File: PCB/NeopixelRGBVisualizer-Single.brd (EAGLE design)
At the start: 26.8 x 29.6 mm, 19 parts, among them IC1 MSGEQ7, Q1 16MHz, X1 STEREOJACK, X2 1751251

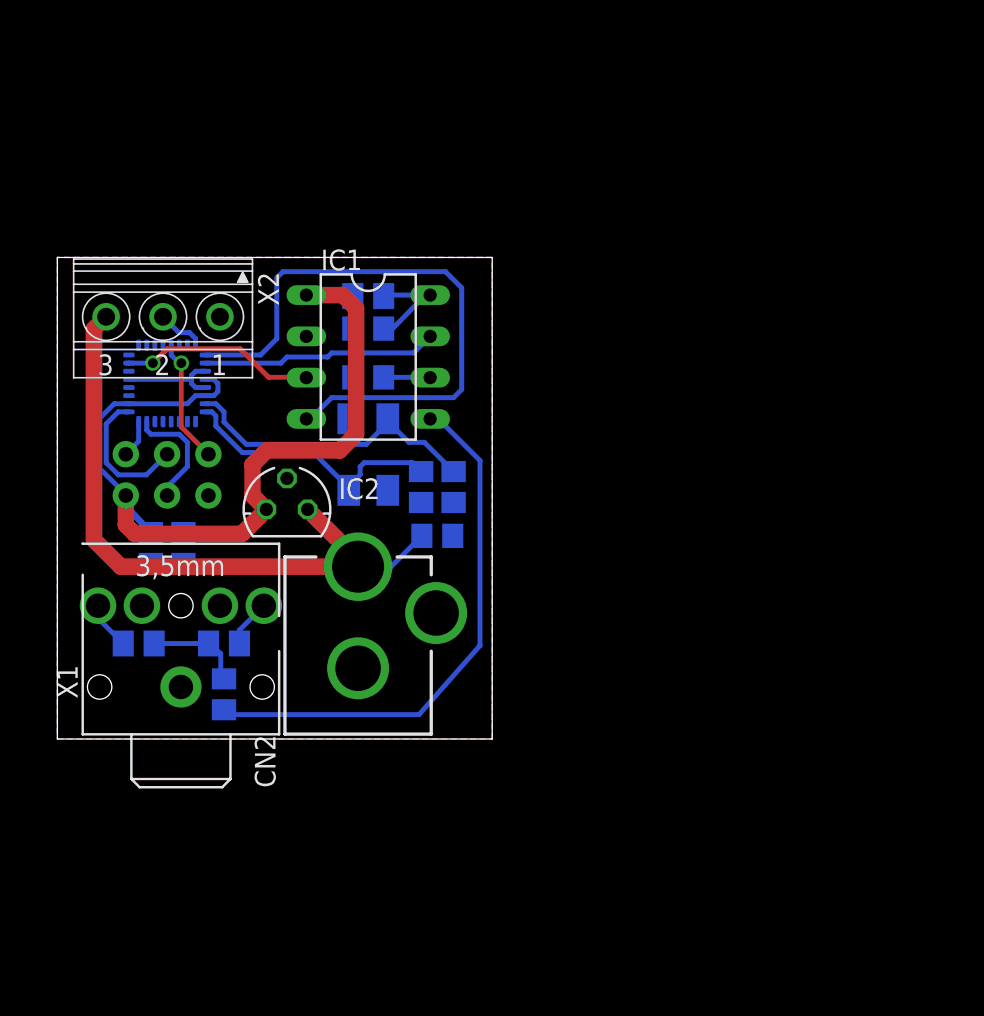
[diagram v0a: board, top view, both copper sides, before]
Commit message: Almost ready for second prototype order -Added 3 tactile buttons for control inputs: "Power","+","-" -Changed Phoenix screw terminal to Molex Mini-Fit Jr receptacle -Added small potentiometer as input volume control -Aligned receptacles with board edge
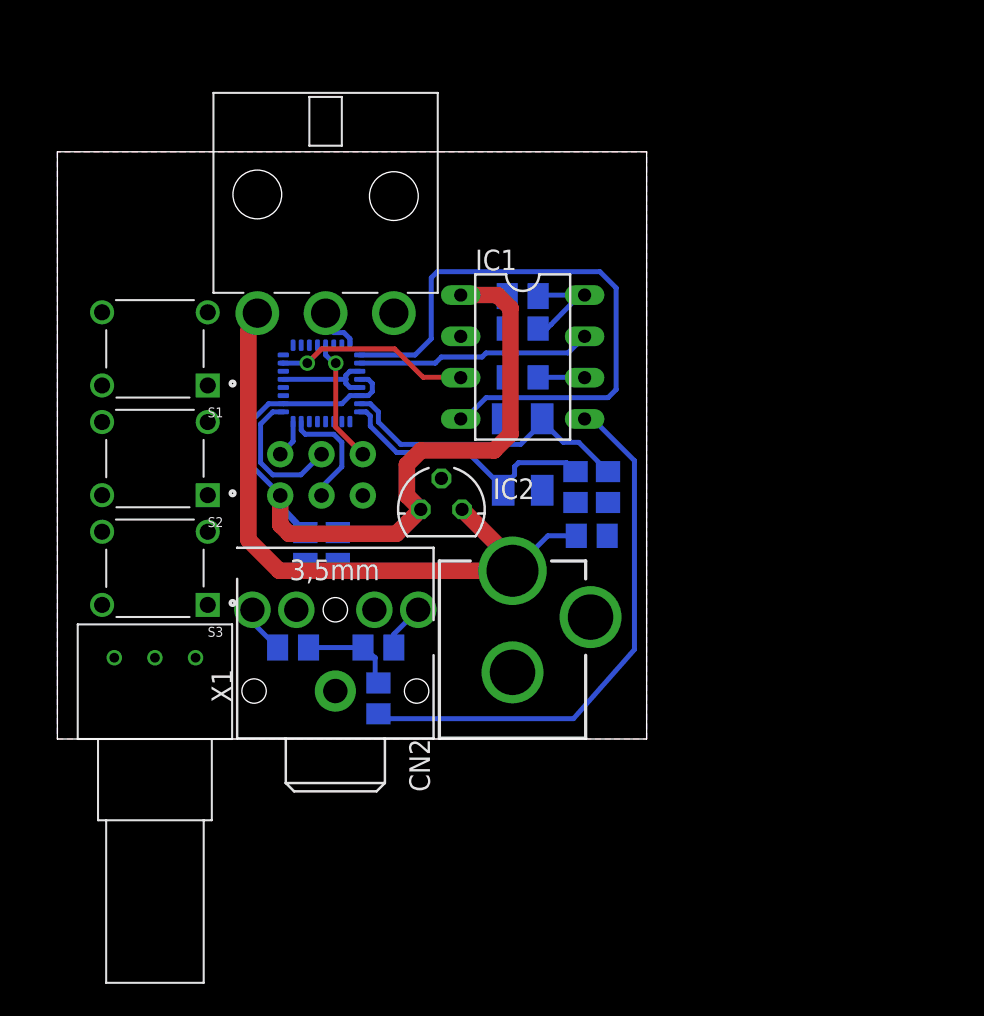
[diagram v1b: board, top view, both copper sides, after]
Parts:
- removed X2: 1751251, con-phoenix-350:1751251
- added S1, S2, S3: 2-1825910-7, 2-1825910-7:SW_2-1825910-7
- added U$2: PTD901-2015K, potentiometers:PTD901-2015K-####
- added U$3: 0039303035, MinifitJR:4.2MM-3PIN
- moved C1 9.50 mm to (19.8, 2.50)
- moved CN2 9.50 mm to (28.0, -3.25)
- moved R1 9.50 mm to (19.8, 5.62)
- moved R2 9.50 mm to (14.5, 5.62)
- moved X1 9.50 mm to (17.0, 0.25)
- moved C2 9.50 mm to (28.6, 25.2)
- moved C3 9.50 mm to (17.2, 11.8)
- moved C4 9.50 mm to (28.6, 22.2)
- moved C5 9.50 mm to (33.9, 15.5)
- moved C6 9.50 mm to (31.9, 15.5)
- moved C7 9.50 mm to (15.2, 11.8)
- moved C8 9.50 mm to (32.9, 12.5)
- moved IC1 9.50 mm to (28.6, 23.5)
- moved IC2 9.50 mm to (23.6, 14.1)
- moved ISP1 9.50 mm to (16.2, 16.2)
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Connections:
- new net N$16: C1.1, U$2.P$2
- new net N$18: S1.1, S1.2
- new net N$19: S2.1, S2.2
- new net N$20: S3.1, S3.2
- net GND: now also S1.3, S1.4, S2.3, S2.4, S3.3, S3.4, U$2.P$1, U$3.P$3; no longer X2.1
- net N$17: now also U$3.P$2; no longer X2.2
- net N$6: now also U$2.P$3; no longer C1.1
- net VIN: now also U$3.P$1; no longer X2.3
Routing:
- net N$17: track 2.96 -> 1.58 mm
- net VIN: track 40.5 -> 39.9 mm
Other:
- board size 26.8 x 29.6 mm -> 36.2 x 36.1 mm

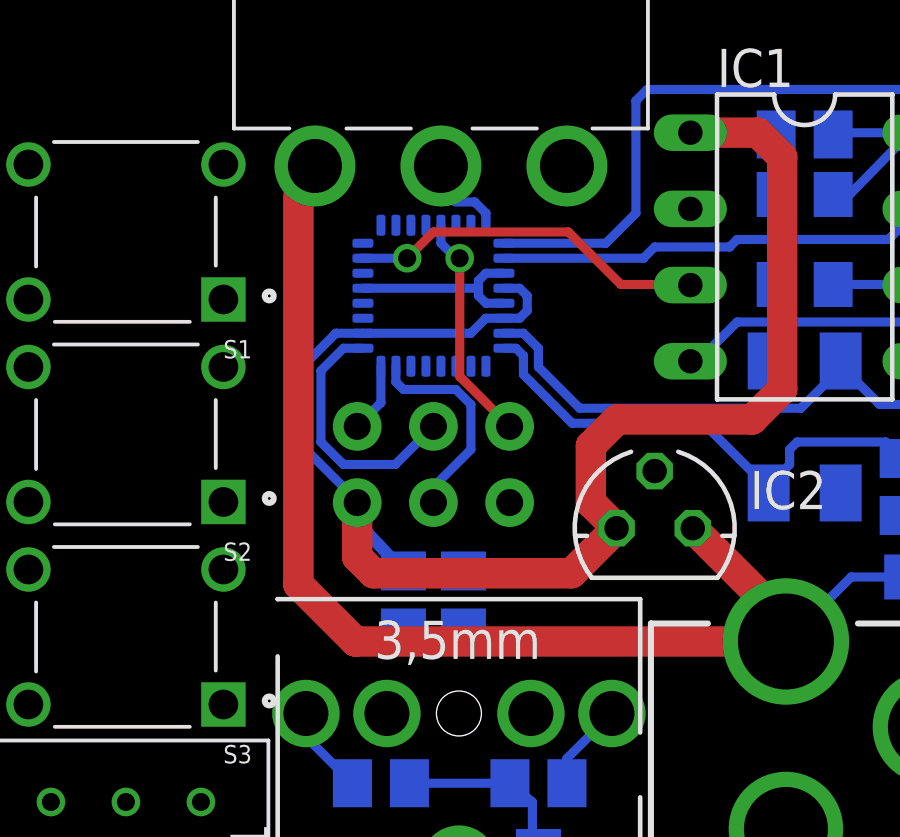
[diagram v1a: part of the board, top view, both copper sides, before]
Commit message: Reverted to first prototype, designing second prototype using updated libraries.
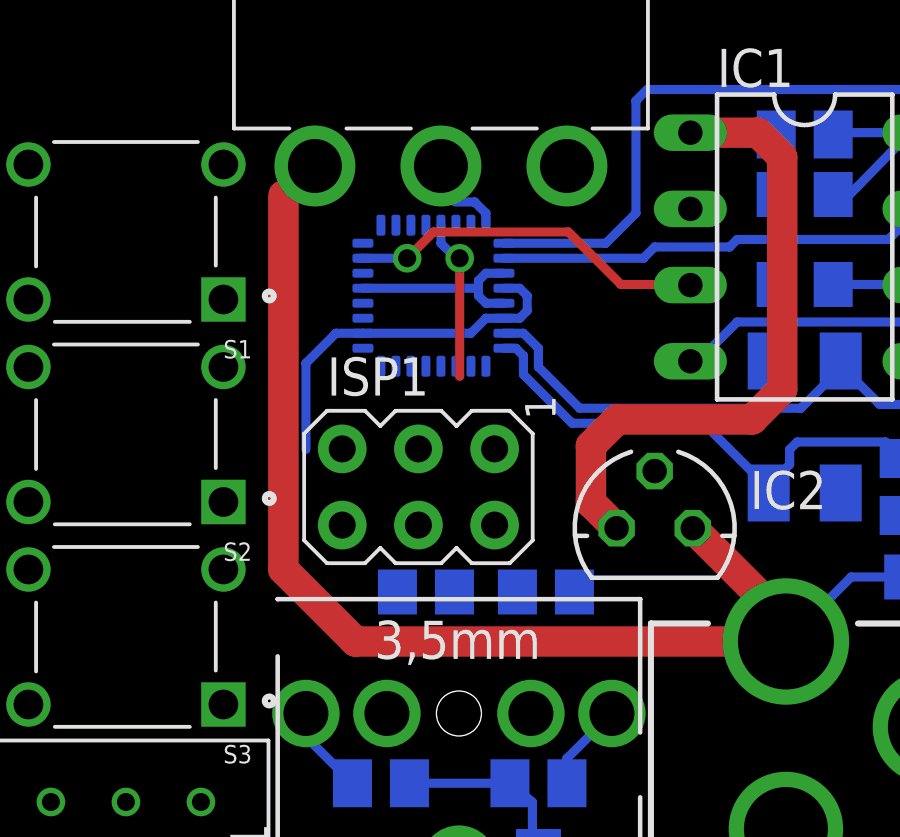
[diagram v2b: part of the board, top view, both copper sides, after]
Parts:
- moved C3 2.76 mm to (20.0, 12.0), turned to 180 degrees
- moved ISP1 0.90 mm to (15.8, 15.5), flipped to the top
- moved C7 0.79 mm to (16.0, 12.0), turned to 0 degrees
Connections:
- net N$18: now also U$1.11
- net N$19: now also U$1.10
- net N$20: now also U$1.9
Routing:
- net VCC: track 53.4 -> 36.7 mm
- net N$1: track 8.67 -> 0.00 mm
- net N$4: track 7.12 -> 0.00 mm
- net N$2: track 7.73 -> 5.37 mm
- net N$3: track 2.33 -> 0.00 mm
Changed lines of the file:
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@@
 <attribute name="VALUE" x="29.895" y="22.71" size="1.27" layer="28" rot="MR0"/>
 </element>
-<element name="C3" library="rcl" package="C0805" value="0.1u" x="17.25" y="11.75" rot="MR270">
-<attribute name="NAME" x="15.98" y="13.02" size="1.27" layer="26" rot="MR270"/>
-<attribute name="VALUE" x="19.79" y="13.02" size="1.27" layer="28" rot="MR270"/>
+<element name="C3" library="rcl" package="C0805" value="0.1u" x="20" y="12" rot="MR180">
+<attribute name="NAME" x="18.73" y="10.73" size="1.27" layer="26" rot="MR180"/>
+<attribute name="VALUE" x="18.73" y="14.54" size="1.27" layer="28" rot="MR180"/>
 </element>
 <element name="C4" library="rcl" package="C0805" value="0.1u" x="28.625" y="22.25" rot="MR0">
@@
 <attribute name="VALUE" x="29.335" y="14.23" size="1.27" layer="28" rot="MR90"/>
 </element>
-<element name="C7" library="rcl" package="C0805" value="0.1u" x="15.25" y="11.75" rot="MR270">
-<attribute name="NAME" x="13.98" y="13.02" size="1.27" layer="26" rot="MR270"/>
-<attribute name="VALUE" x="17.79" y="13.02" size="1.27" layer="28" rot="MR270"/>
+<element name="C7" library="rcl" package="C0805" value="0.1u" x="16" y="12" rot="MR0">
+<attribute name="NAME" x="17.27" y="13.27" size="1.27" layer="26" rot="MR0"/>
+<attribute name="VALUE" x="17.27" y="9.46" size="1.27" layer="28" rot="MR0"/>
 </element>
 <element name="CN2" library="adafruit" package="DCJACK_2MM_PTH" value="" x="28" y="-3.25">
@@
 <attribute name="VALUE" x="27.99" y="27.056" size="1.27" layer="27" ratio="10" rot="R270"/>
 </element>
-<element name="ISP1" library="adafruit" package="AVRISP" value="AVRISP-6" x="16.25" y="16.25" rot="MR270">
-<attribute name="NAME" x="19.298" y="19.298" size="1.27" layer="26" rot="MR0"/>
+<element name="ISP1" library="adafruit" package="AVRISP" value="AVRISP-6" x="15.75" y="15.5" rot="R270">
+<attribute name="NAME" x="12.702" y="18.548" size="1.27" layer="25"/>
 </element>
 <element name="Q1" library="adafruit" package="CTS406" value="16MHz" x="28.625" y="17.5" rot="MR270">
@@
 <contactref element="U$1" pad="17"/>
 <contactref element="ISP1" pad="3"/>
-<wire x1="13.9" y1="20.125" x2="13.25" y2="20.125" width="0.3048" layer="16"/>
-<wire x1="13.25" y1="20.125" x2="12.5" y2="19.375" width="0.3048" layer="16"/>
-<wire x1="12.5" y1="19.375" x2="12.5" y2="17" width="0.3048" layer="16"/>
-<wire x1="16.25" y1="17.52" x2="14.98" y2="16.25" width="0.3048" layer="16"/>
-<wire x1="13.25" y1="16.25" x2="12.5" y2="17" width="0.3048" layer="16"/>
-<wire x1="14.98" y1="16.25" x2="13.25" y2="16.25" width="0.3048" layer="16"/>
+<wire x1="15.75" y1="16.77" x2="13.9" y2="20.125" width="0" layer="19" extent="16-16"/>
 </signal>
 <signal name="N$2">
@@
 <wire x1="16.5" y1="24.225" x2="16.5" y2="23.625" width="0.3048" layer="16"/>
 <wire x1="17.125" y1="23.125" x2="17.125" y2="19.185" width="0.3048" layer="1"/>
-<wire x1="18.79" y1="17.52" x2="17.125" y2="19.185" width="0.3048" layer="1"/>
+<wire x1="17.125" y1="19.185" x2="13.21" y2="16.77" width="0" layer="19" extent="1-1"/>
 </signal>
 <signal name="N$3">
 <contactref element="U$1" pad="16"/>
 <contactref element="ISP1" pad="1"/>
-<wire x1="14.5" y1="19.525" x2="14.5" y2="18.31" width="0.3048" layer="16"/>
-<wire x1="14.5" y1="18.31" x2="13.71" y2="17.52" width="0.3048" layer="16"/>
+<wire x1="18.29" y1="16.77" x2="14.5" y2="19.525" width="0" layer="19" extent="16-16"/>
 </signal>
 <signal name="N$4">
 <contactref element="ISP1" pad="4"/>
 <contactref element="U$1" pad="15"/>
-<wire x1="16.25" y1="15.5" x2="16.25" y2="14.98" width="0.3048" layer="16"/>
-<wire x1="17.5" y1="16.75" x2="16.25" y2="15.5" width="0.3048" layer="16"/>
-<wire x1="17.5" y1="18.25" x2="17.5" y2="16.75" width="0.3048" layer="16"/>
-<wire x1="17.5" y1="18.25" x2="17" y2="18.75" width="0.3048" layer="16"/>
-<wire x1="17" y1="18.75" x2="15.25" y2="18.75" width="0.3048" layer="16"/>
-<wire x1="15.25" y1="18.75" x2="15" y2="19" width="0.3048" layer="16"/>
-<wire x1="15" y1="19.525" x2="15" y2="19" width="0.3048" layer="16"/>
+<wire x1="15.75" y1="14.23" x2="15" y2="19.525" width="0" layer="19" extent="16-16"/>
 </signal>
 <signal name="N$7">
@@
 <contactref element="CN2" pad="PWR"/>
 <contactref element="C8" pad="1"/>
-<wire x1="13.65" y1="10.35" x2="11.75" y2="12.25" width="1.016" layer="1"/>
+<wire x1="13.65" y1="10.35" x2="11.25" y2="12.75" width="1.016" layer="1"/>
 <wire x1="28" y1="10.35" x2="13.65" y2="10.35" width="1.016" layer="1"/>
-<wire x1="11.75" y1="25.225" x2="11.75" y2="12.25" width="1.016" layer="1"/>
+<wire x1="11.25" y1="25.225" x2="11.25" y2="12.75" width="1.016" layer="1"/>
 <contactref element="IC2" pad="IN"/>
 <wire x1="28.025" y1="10.35" x2="28" y2="10.35" width="0.3048" layer="16"/>
@@
 <wire x1="28" y1="11.02" x2="24.895" y2="14.125" width="1.016" layer="1"/>
 <contactref element="U$3" pad="P$1"/>
-<wire x1="12.3" y1="26.2" x2="11.75" y2="12.25" width="0" layer="19" extent="1-1"/>
+<wire x1="12.3" y1="26.2" x2="11.25" y2="12.75" width="0" layer="19" extent="1-1"/>
 </signal>
 <signal name="GND">
@@
 <wire x1="27.675" y1="22.25" x2="27.675" y2="25.25" width="0" layer="19" extent="16-16"/>
 <wire x1="18.6" y1="22.625" x2="24.815" y2="24.77" width="0" layer="19" extent="16-16"/>
-<wire x1="18.79" y1="14.98" x2="18.6" y2="21.625" width="0" layer="19" extent="16-16"/>
-<wire x1="17.25" y1="10.8" x2="18.79" y2="14.98" width="0" layer="19" extent="16-16"/>
-<wire x1="15.25" y1="10.8" x2="17.25" y2="10.8" width="0" layer="19" extent="16-16"/>
-<wire x1="23.625" y1="16.03" x2="18.79" y2="14.98" width="0" layer="19" extent="1-1"/>
-<wire x1="17.1" y1="2.95" x2="17.25" y2="10.8" width="0" layer="19" extent="16-16"/>
+<wire x1="13.21" y1="14.23" x2="18.6" y2="21.625" width="0" layer="19" extent="16-16"/>
+<wire x1="20.95" y1="12" x2="13.21" y2="14.23" width="0" layer="19" extent="16-16"/>
+<wire x1="15.05" y1="12" x2="20.95" y2="12" width="0" layer="19" extent="16-16"/>
+<wire x1="23.625" y1="16.03" x2="13.21" y2="14.23" width="0" layer="19" extent="1-1"/>
+<wire x1="17.1" y1="2.95" x2="20.95" y2="12" width="0" layer="19" extent="16-16"/>
 <wire x1="31.875" y1="14.55" x2="23.625" y2="16.03" width="0" layer="19" extent="16-16"/>
 <wire x1="33.875" y1="14.55" x2="31.875" y2="14.55" width="0" layer="19" extent="16-16"/>
@@
 <wire x1="13" y1="20.625" x2="12" y2="19.625" width="0.3048" layer="16"/>
 <wire x1="13.9" y1="20.625" x2="13" y2="20.625" width="0.3048" layer="16"/>
-<wire x1="13.71" y1="15.04" x2="13.71" y2="14.98" width="0.3048" layer="16"/>
-<wire x1="13.71" y1="15.04" x2="12" y2="16.75" width="0.3048" layer="16"/>
 <wire x1="12" y1="19.625" x2="12" y2="16.75" width="0.3048" layer="16"/>
 <wire x1="18.6" y1="21.125" x2="18" y2="21.125" width="0.3048" layer="16"/>
 <wire x1="18" y1="21.125" x2="17.5" y2="20.625" width="0.3048" layer="16"/>
 <wire x1="17.5" y1="20.625" x2="13.9" y2="20.625" width="0.3048" layer="16"/>
-<wire x1="15.25" y1="12.7" x2="13.71" y2="14.34" width="0.4064" layer="16"/>
-<wire x1="13.71" y1="14.98" x2="13.71" y2="14.34" width="0.4064" layer="16"/>
 <wire x1="19.125" y1="22.125" x2="18.6" y2="22.125" width="0.3048" layer="16"/>
 <wire x1="19.375" y1="21.875" x2="19.125" y2="22.125" width="0.3048" layer="16"/>
@@
 <wire x1="24.875" y1="27.25" x2="24.815" y2="27.31" width="0.8128" layer="1"/>
 <contactref element="IC2" pad="OUT"/>
-<wire x1="13.71" y1="14.98" x2="13.71" y2="13.165" width="1.016" layer="1"/>
-<wire x1="14.25" y1="12.625" x2="13.71" y2="13.165" width="1.016" layer="1"/>
-<wire x1="20.855" y1="12.625" x2="14.25" y2="12.625" width="1.016" layer="1"/>
-<wire x1="22.355" y1="14.125" x2="20.855" y2="12.625" width="1.016" layer="1"/>
 <wire x1="27.065" y1="27.31" x2="24.815" y2="27.31" width="1.016" layer="1"/>
 <wire x1="27.875" y1="26.5" x2="27.065" y2="27.31" width="1.016" layer="1"/>
@@
 <wire x1="21.5" y1="16.875" x2="21.5" y2="14.98" width="1.016" layer="1"/>
 <wire x1="22.355" y1="14.125" x2="21.5" y2="14.98" width="1.016" layer="1"/>
-<wire x1="13.71" y1="14.34" x2="17.25" y2="12.7" width="0" layer="19" extent="16-16"/>
+<wire x1="19.375" y1="21.375" x2="22.375" y2="17.75" width="0" layer="19" extent="1-16"/>
+<wire x1="18.29" y1="14.23" x2="12" y2="16.75" width="0" layer="19" extent="16-16"/>
+<wire x1="16.95" y1="12" x2="18.29" y2="14.23" width="0" layer="19" extent="16-16"/>
+<wire x1="19.05" y1="12" x2="16.95" y2="12" width="0" layer="19" extent="16-16"/>
 </signal>
 <signal name="N$16">
@@
 <contactref element="S1" pad="1"/>
 <contactref element="S1" pad="2"/>
+<contactref element="U$1" pad="11"/>
 <wire x1="9.25" y1="21.75" x2="9.25" y2="26.25" width="0" layer="19" extent="1-1"/>
+<wire x1="17" y1="19.525" x2="9.25" y2="21.75" width="0" layer="19" extent="16-16"/>
 </signal>
 <signal name="N$19">
 <contactref element="S2" pad="1"/>
 <contactref element="S2" pad="2"/>
+<contactref element="U$1" pad="10"/>
+<wire x1="9.25" y1="19.5" x2="17.5" y2="19.525" width="0" layer="19" extent="16-16"/>
 <wire x1="9.25" y1="15" x2="9.25" y2="19.5" width="0" layer="19" extent="1-1"/>
 </signal>
@@
 <contactref element="S3" pad="1"/>
 <contactref element="S3" pad="2"/>
+<contactref element="U$1" pad="9"/>
+<wire x1="9.25" y1="12.75" x2="18" y2="19.525" width="0" layer="19" extent="16-16"/>
 <wire x1="9.25" y1="8.25" x2="9.25" y2="12.75" width="0" layer="19" extent="1-1"/>
 </signal>
